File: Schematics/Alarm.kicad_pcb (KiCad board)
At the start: 2 copper layers, 116.8 x 63.5 mm, 5 parts, among them SW1 SW_MEC_5G_LED, U3 BluetoothModule

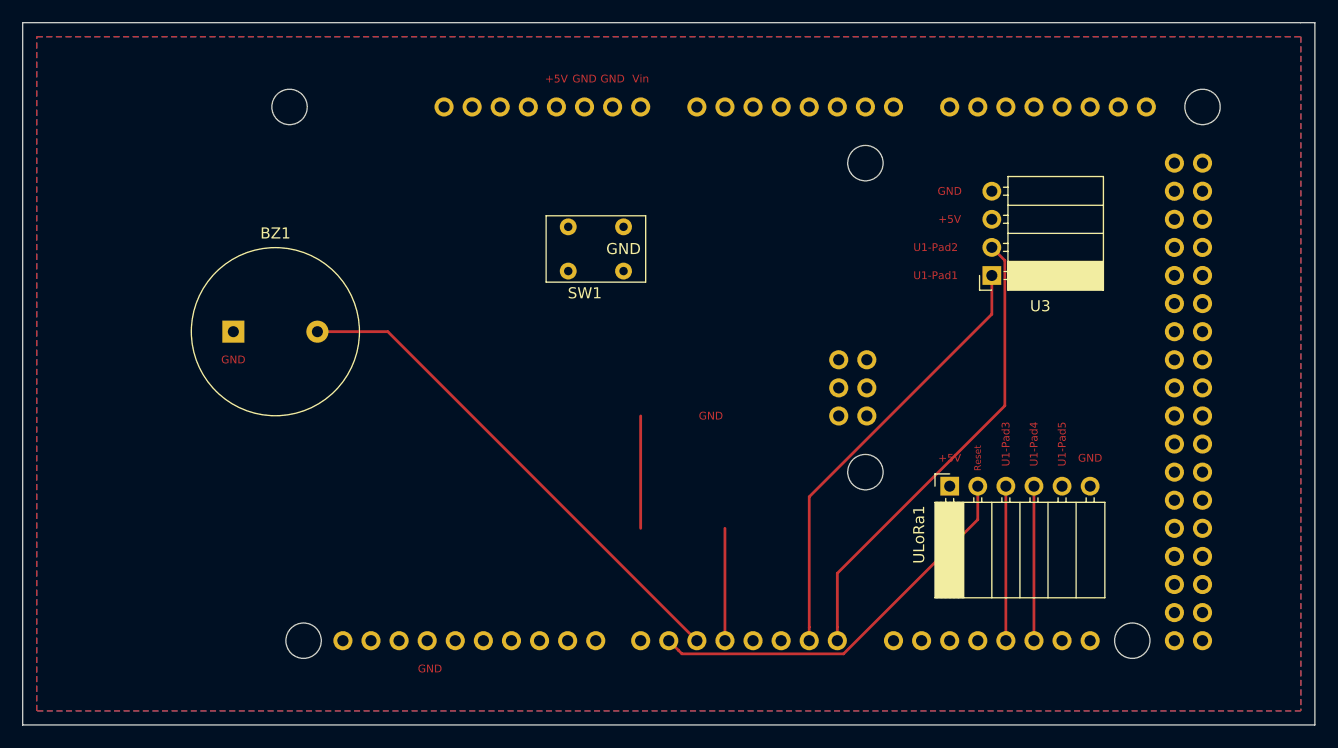
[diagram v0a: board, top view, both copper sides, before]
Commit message: Surface Changes And Button Retracking
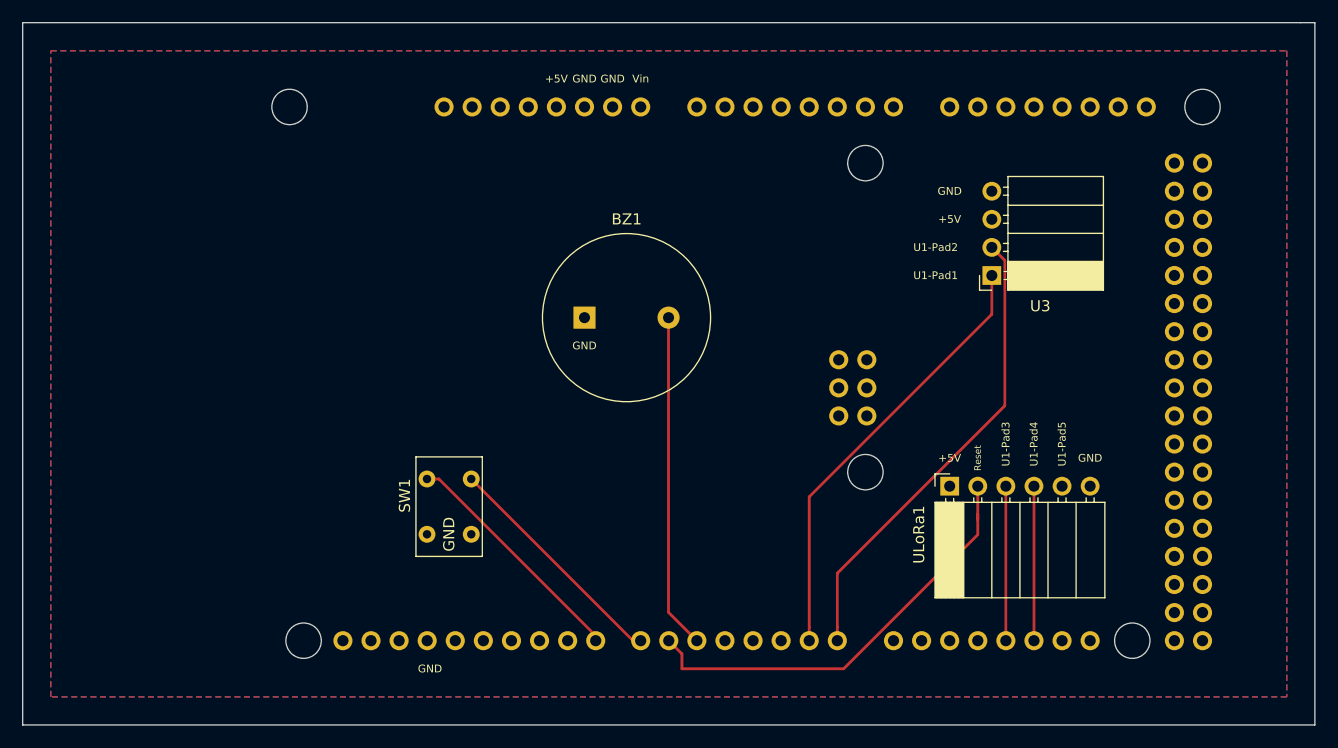
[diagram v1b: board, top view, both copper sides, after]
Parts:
- moved SW1 32.3 mm to (100.3, 88.9), turned to 90 degrees
- moved BZ1 31.8 mm to (115.6, 67.3)
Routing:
- net Net-(SW1-Pad4): track 0.00 -> 21.6 mm
- net Net-(SW1-Pad3): track 0.00 -> 21.4 mm
- net Net-(BZ1-Pad2): track 45.9 -> 30.3 mm
- net Net-(D_RED1-Pad2): track 10.2 -> 0.00 mm
- net (no net): track 10.2 -> 0.00 mm
- net Lora_Reset: track 36.5 -> 39.7 mm
- added copper zone on B.Cu, net +5V
- added copper zone on F.Cu, net GND
- removed copper zone on F.Cu, net +5V
- removed copper zone on B.Cu, net GND
